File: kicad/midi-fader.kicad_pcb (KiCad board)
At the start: 2 copper layers, 73.7 x 78.7 mm, 167 parts, among them J1 SWD, J2 EXTERNAL_OUT, J3 EXTERNAL_IN, J4 USB_OTG, SW1 TR2-21-L5, SW2 TR2-21-L5, U1 STM32F042KxT, U2 USBLC6-2, U3 MCP1603, U4 MIC2776L, U5 MIC5501-XYM5, U6 74HC165, U7 STP08DP05

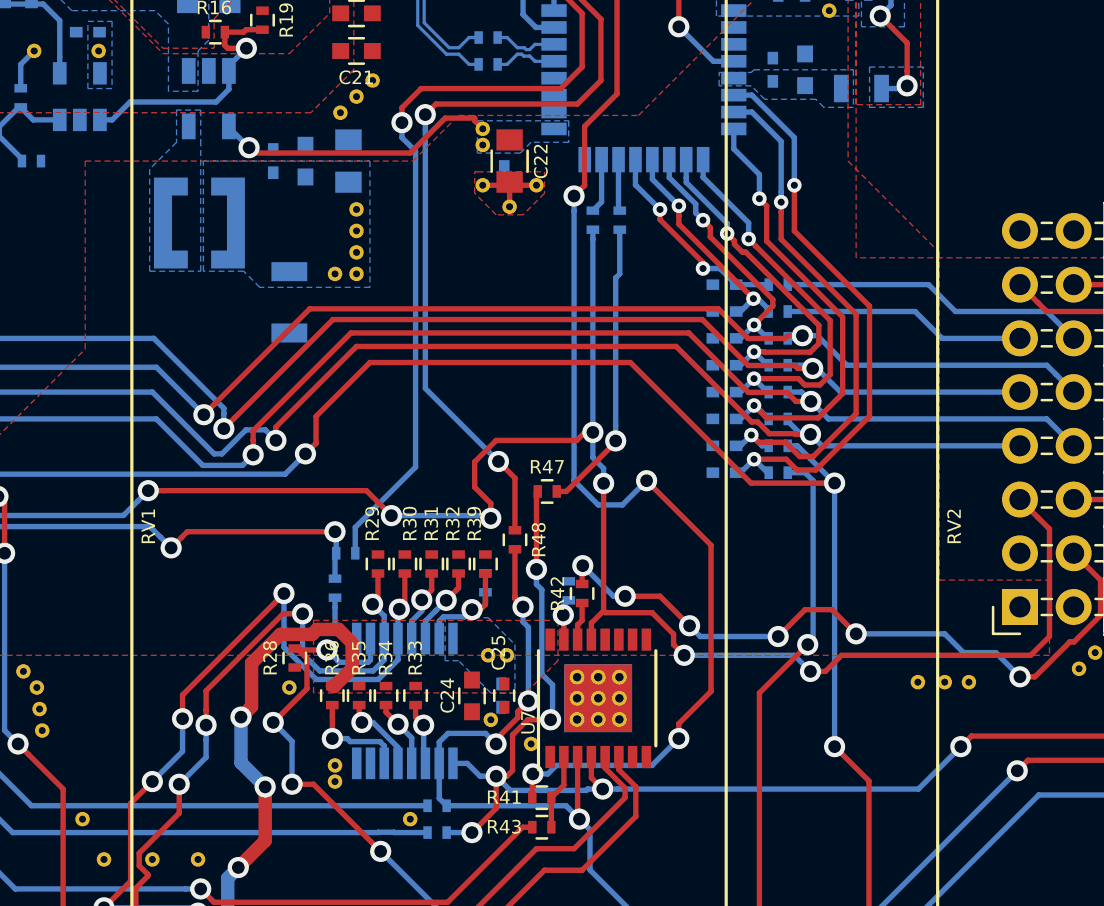
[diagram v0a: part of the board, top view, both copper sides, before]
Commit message: Fixed NPTH on the sliders
Those are not supposed to be non-plated. Whoops.
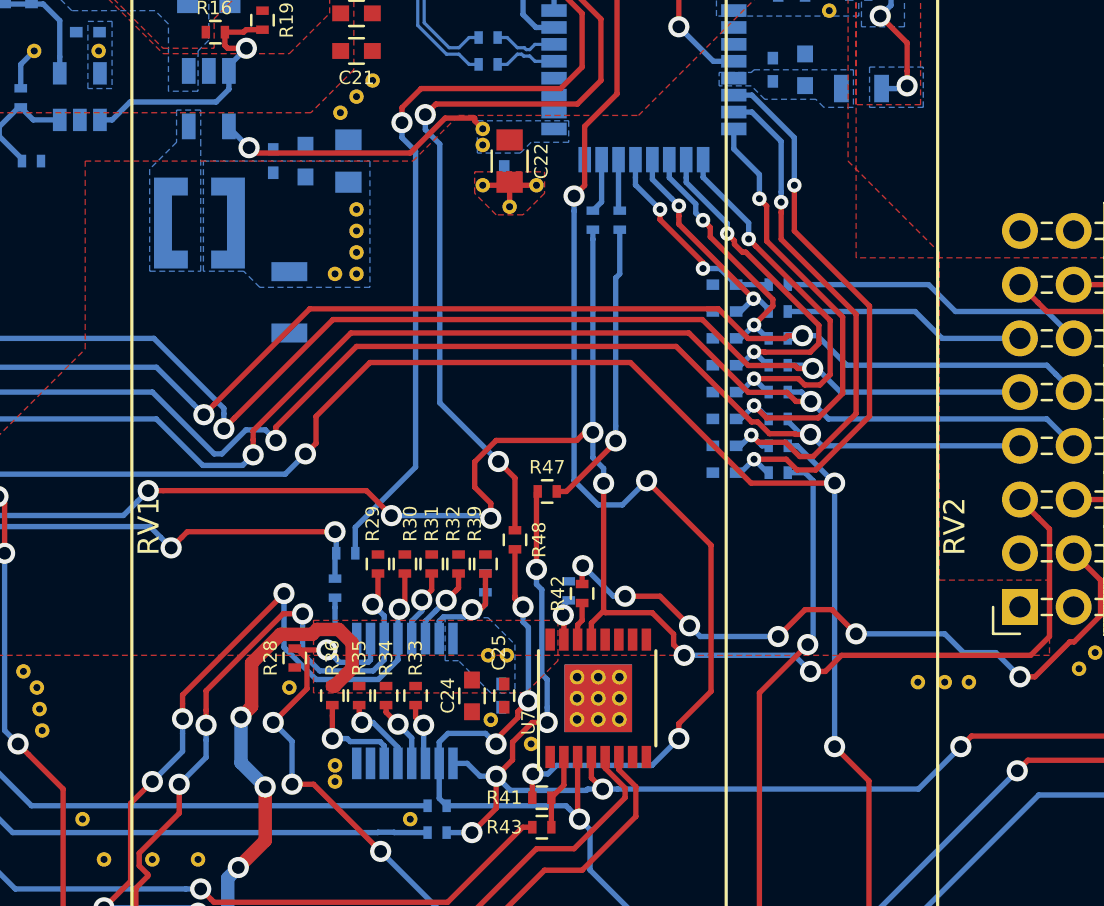
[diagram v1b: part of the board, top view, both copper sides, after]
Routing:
- net /Input/LCLK_LCL: track 84.8 -> 84.0 mm
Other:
- rule pad_to_mask_clearance: 0.1524 -> 0.0762
